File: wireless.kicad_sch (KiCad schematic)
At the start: 37 parts, among them J1301 u.FL, U1301 LBEE5KL1YN-814

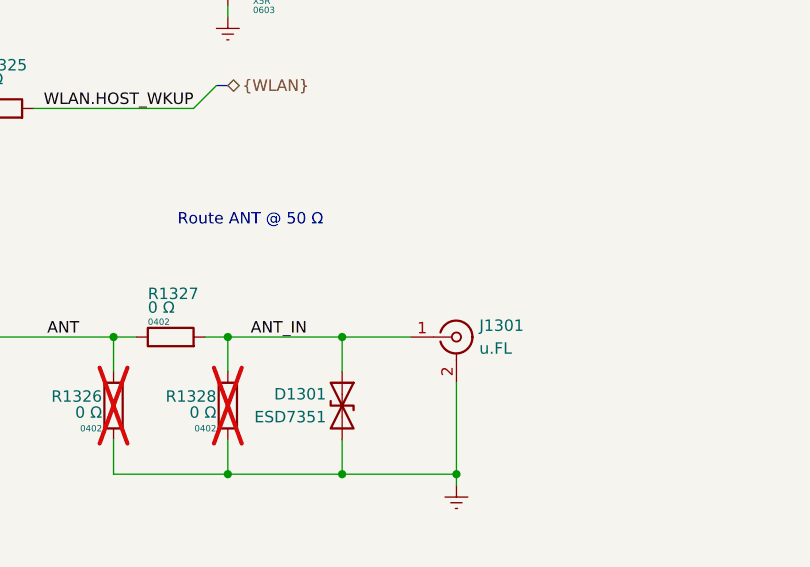
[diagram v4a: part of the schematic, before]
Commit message: Fill BOM information for the rest
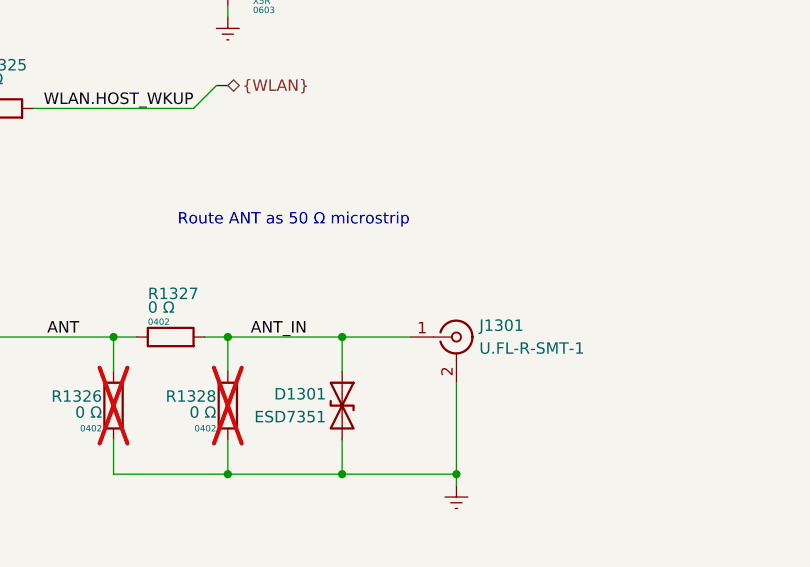
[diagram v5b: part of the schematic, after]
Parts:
- J1301: value u.FL -> U.FL-R-SMT-1; footprint (none) -> Connector_Coaxial:U.FL_Hirose_U.FL-R-SMT-1_Vertical; Digi-Key Part Number (none) -> H11891CT-ND; MPN (none) -> U.FL-R-SMT-1(10); Manufacturer (none) -> Hirose Electric Co Ltd
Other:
- note added: "Route ANT as 50 Ω microstrip"
- note removed: "Route ANT @ 50 Ω"
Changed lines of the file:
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@@
 		(members "WLAN.D[0..3]" "WLAN.CMD" "WLAN.CLK" "WLAN.REG_ON" "WLAN.HOST_WKUP")
 	)
-	(text "Route ANT @ 50 Ω"
+	(text "Route ANT as 50 Ω microstrip"
 		(exclude_from_sim no)
 		(at 273.812 162.306 0)
@@
 			)
 		)
-		(property "Value" "u.FL"
+		(property "Value" "U.FL-R-SMT-1"
 			(at 307.34 176.53 0)
 			(effects
@@
 			)
 		)
-		(property "Footprint" ""
+		(property "Footprint" "Connector_Coaxial:U.FL_Hirose_U.FL-R-SMT-1_Vertical"
 			(at 304.8 175.26 0)
 			(effects
@@
 			)
 		)
-		(property "Datasheet" "~"
+		(property "Datasheet" "https://mm.digikey.com/Volume0/opasdata/d220001/medias/docus/4832/EDC3-302540-10.tif.pdf"
 			(at 304.8 175.26 0)
 			(effects
@@
 			)
 		)
-		(property "Description" "coaxial connector (BNC, SMA, SMB, SMC, Cinch/RCA, LEMO, ...)"
+		(property "Description" "U.FL (UMCC) Connector Receptacle, Male Pin 50 Ohms Surface Mount Solder"
 			(at 304.8 175.26 0)
 			(effects
+				(font
+					(size 1.27 1.27)
+				)
+				(hide yes)
+			)
+		)
+		(property "Digi-Key Part Number" "H11891CT-ND"
+			(at 304.8 175.26 0)
+			(effects
+				(font
+					(size 1.27 1.27)
+				)
+				(hide yes)
+			)
+		)
+		(property "MPN" "U.FL-R-SMT-1(10)"
+			(at 304.8 175.26 0)
+			(effects
+				(font
+					(size 1.27 1.27)
+				)
+				(hide yes)
+			)
+		)
+		(property "Manufacturer" "Hirose Electric Co Ltd"
+			(at 304.8 175.26 0)
+			(effects

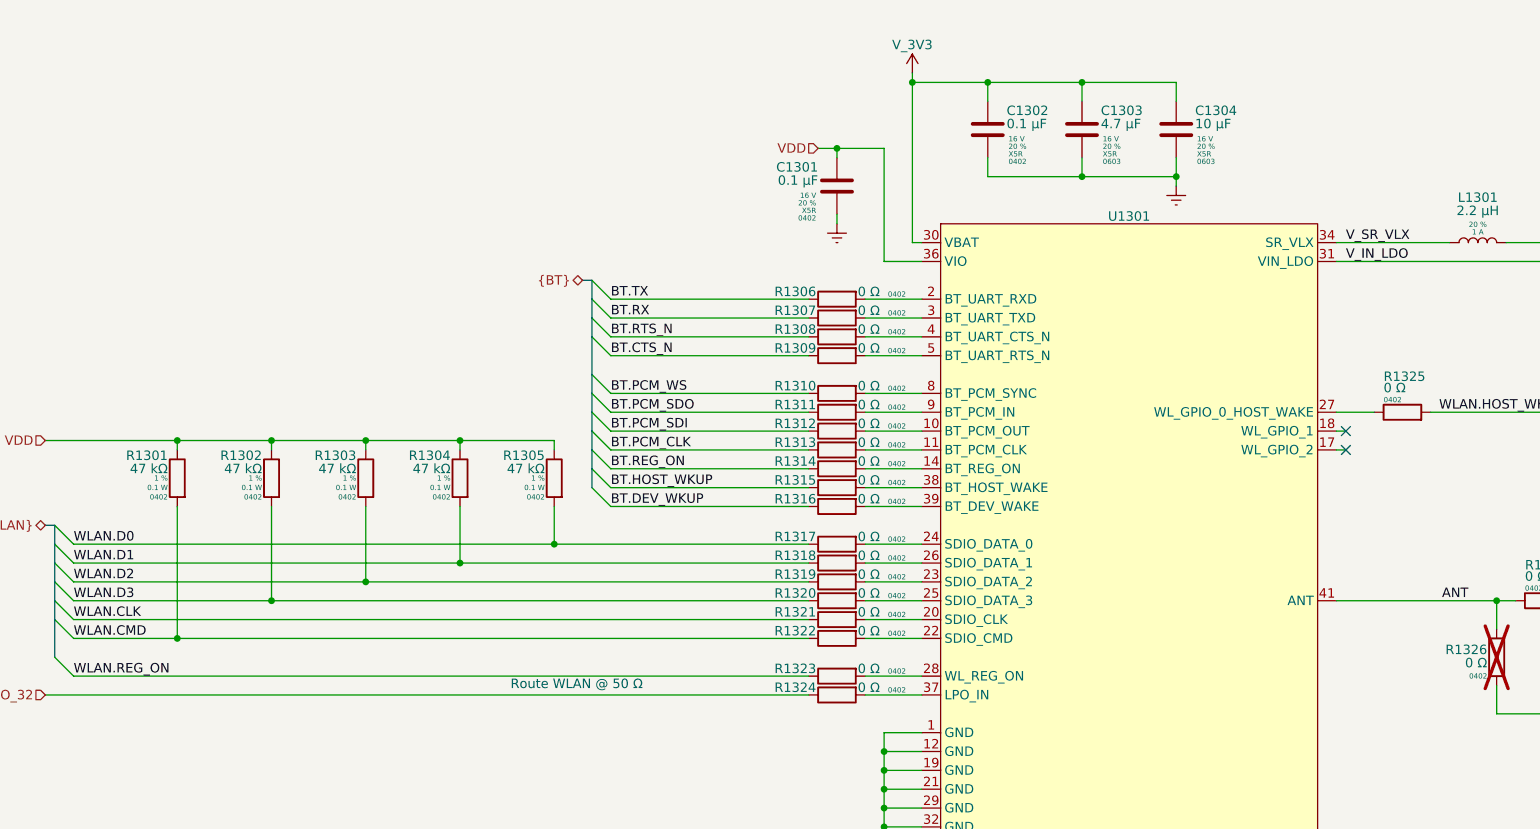
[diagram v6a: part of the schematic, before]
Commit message: 0402 -> 0201 where possible
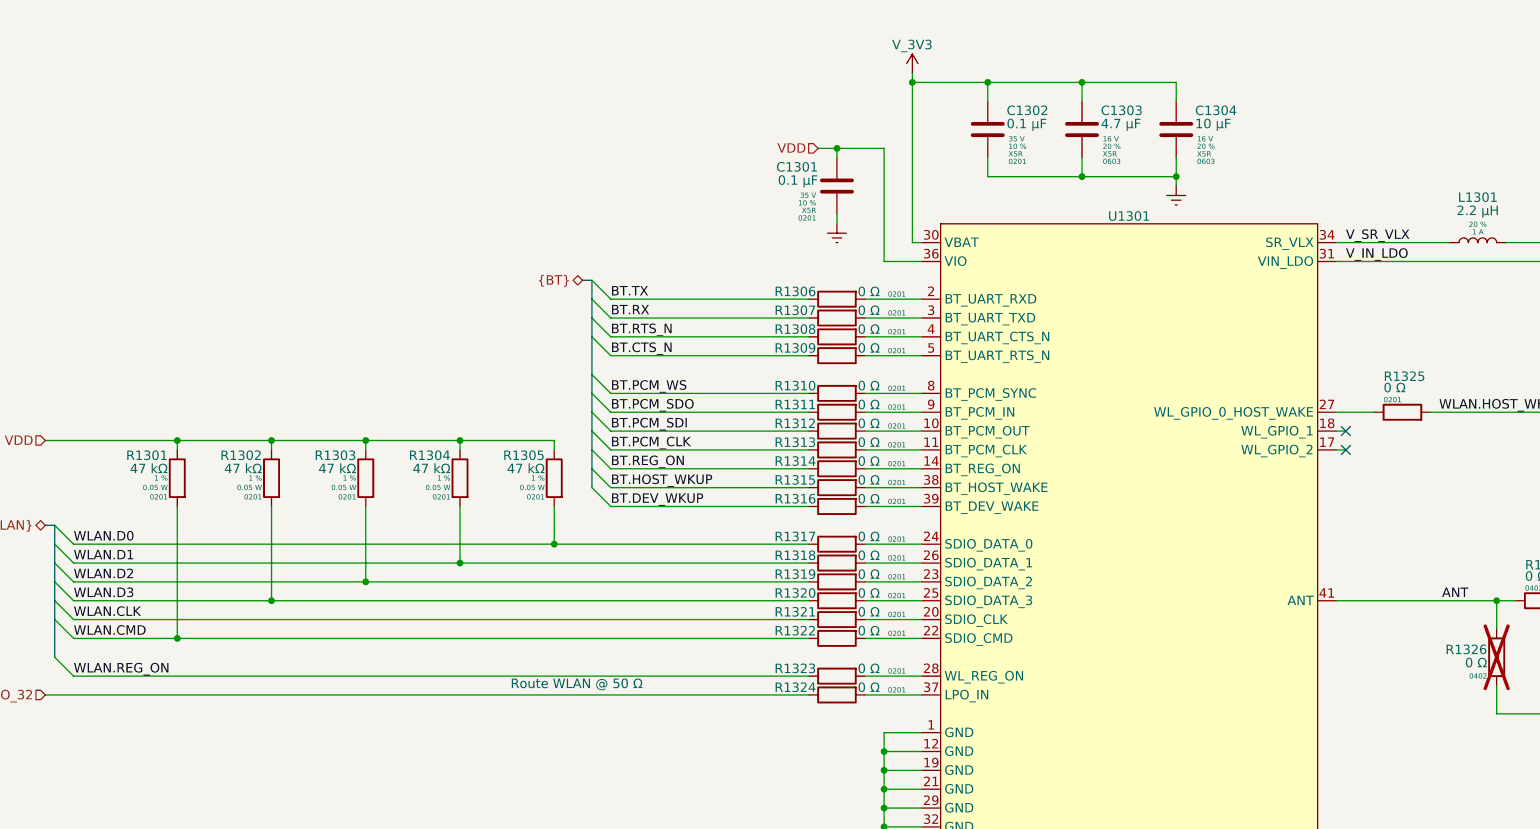
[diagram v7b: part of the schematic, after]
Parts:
- C1301, C1302: footprint perfect_footprints:C_0402_1005Metric -> Capacitor_SMD:C_0201_0603Metric; Digi-Key Part Number 490-10700-1-ND -> 490-10430-1-ND; MPN GRM155R71H104KE14D -> GRM033R6YA104KE14D; Size 0402 -> 0201; Tolerance 20 % -> 10 %; Voltage rating 16 V -> 35 V
- R1301, R1302, R1303, R1304, R1305: footprint perfect_footprints:R_0402_1005Metric -> Resistor_SMD:R_0201_0603Metric; Digi-Key Part Number P47.0KLCT-ND -> P123032CT-ND; MPN ERJ-2RKF4702X -> ERJ-1GNF4702C; Power rating 0.1 W -> 0.05 W; Size 0402 -> 0201
- R1306, R1307, R1308, R1309, R1310, R1311, R1312, R1313, R1314, R1315, R1316, R1317, R1318, R1319, R1320, R1321, R1322, R1323, R1324, R1325: footprint perfect_footprints:R_0402_1005Metric -> Resistor_SMD:R_0201_0603Metric; Digi-Key Part Number P0.0JCT-ND -> P15979CT-ND; MPN ERJ-2GE0R00X -> ERJ-1GN0R00C; Size 0402 -> 0201
